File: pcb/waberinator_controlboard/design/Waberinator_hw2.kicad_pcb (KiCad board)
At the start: 2 copper layers, 104 parts, among them J1 Conn_01x04_Pin, J11 Strang 1, J12 Strang 2, J13 Strang 3, J14 Strang 4, J15 Strang 5, J16 Strang 6, J4 Conn_01x08_Pin, Q1 AOSP21321, Q2 SISHA04DN-T1-GE3, Q3 SISHA04DN-T1-GE3, Q4 SISHA04DN-T1-GE3, Q5 SISHA04DN-T1-GE3, Q6 SISHA04DN-T1-GE3, Q7 SISHA04DN-T1-GE3, SW1 SW_SPDT, SW2 SW_SPDT, U1 STM32F030R8Tx, U2 AMS1117-3.3, U3 LM73606QRNPRQ1, U4 LM75B, U5 MCP14A0304xMNY, U6 MCP14A0304xMNY, U7 MCP14A0304xMNY

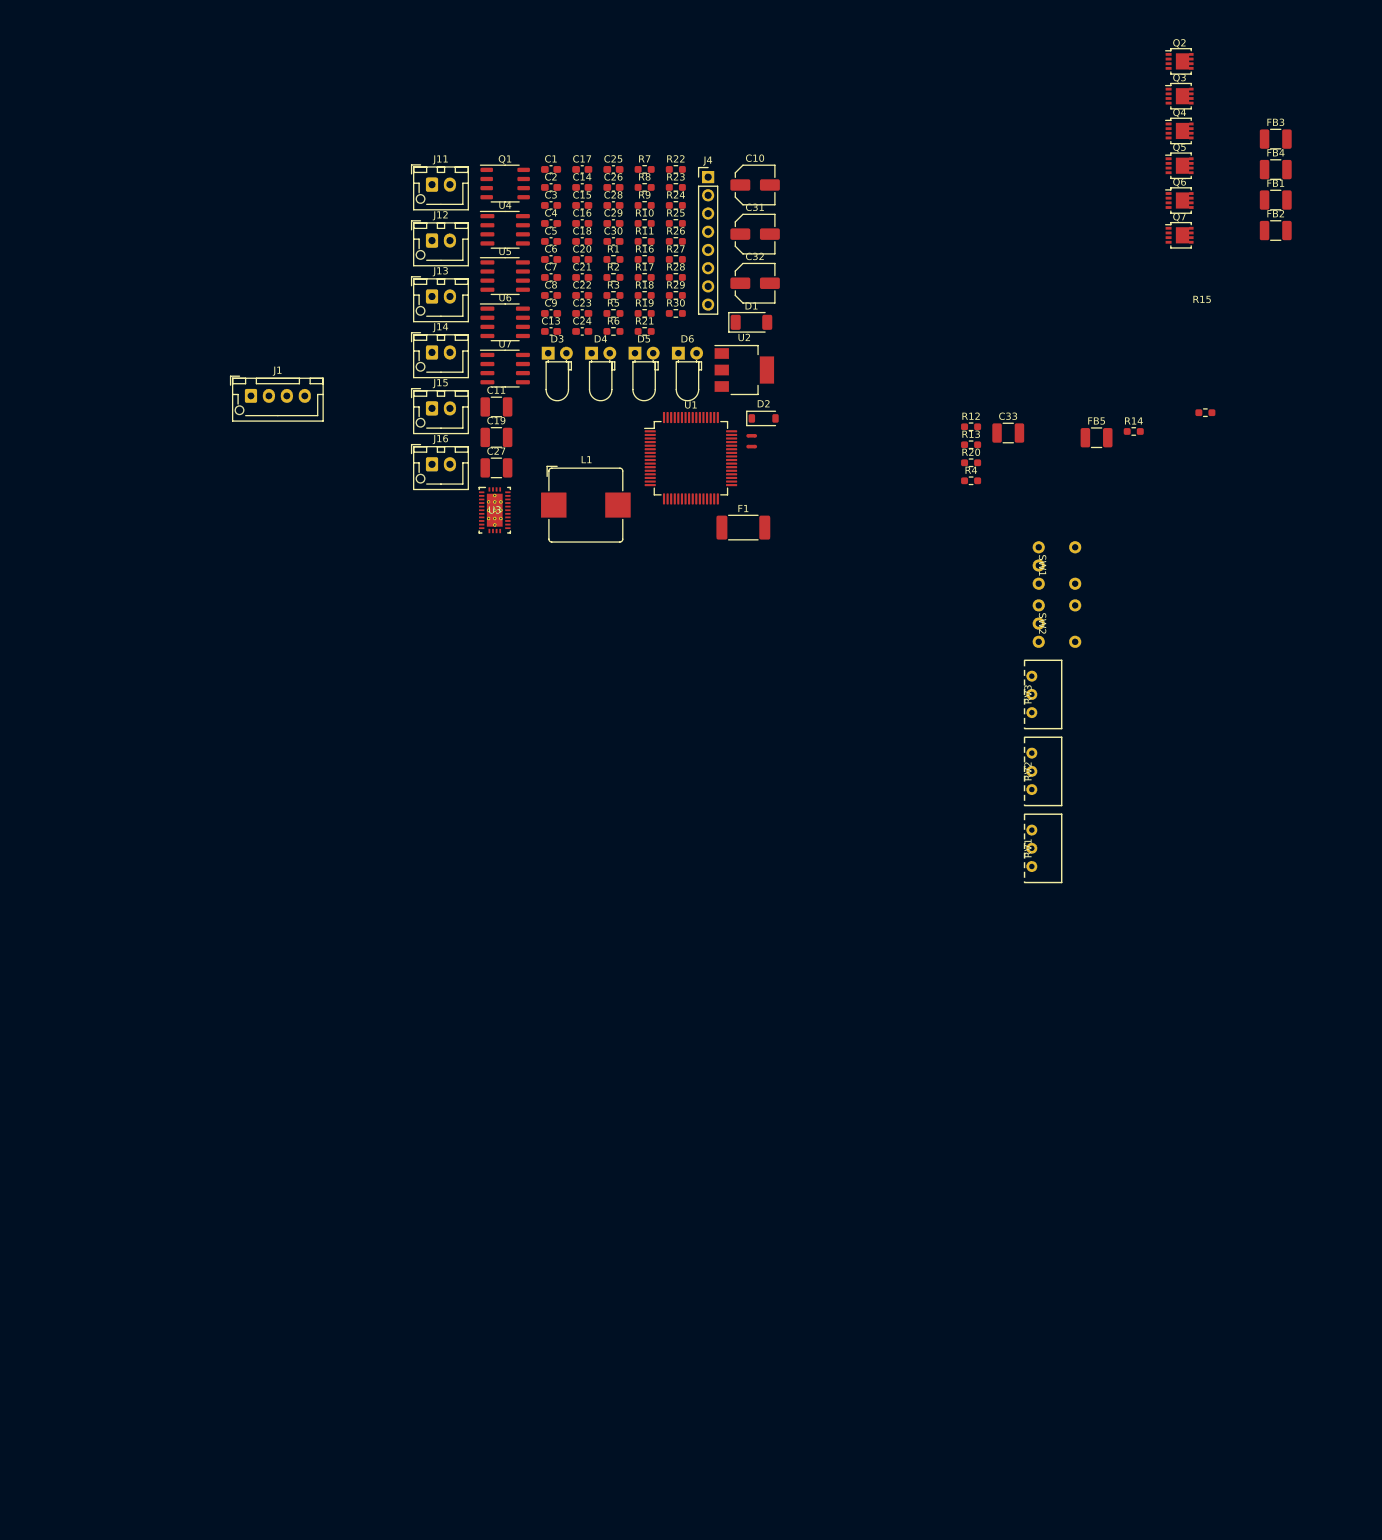
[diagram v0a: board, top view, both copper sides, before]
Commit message: [PCB] components roughly placed
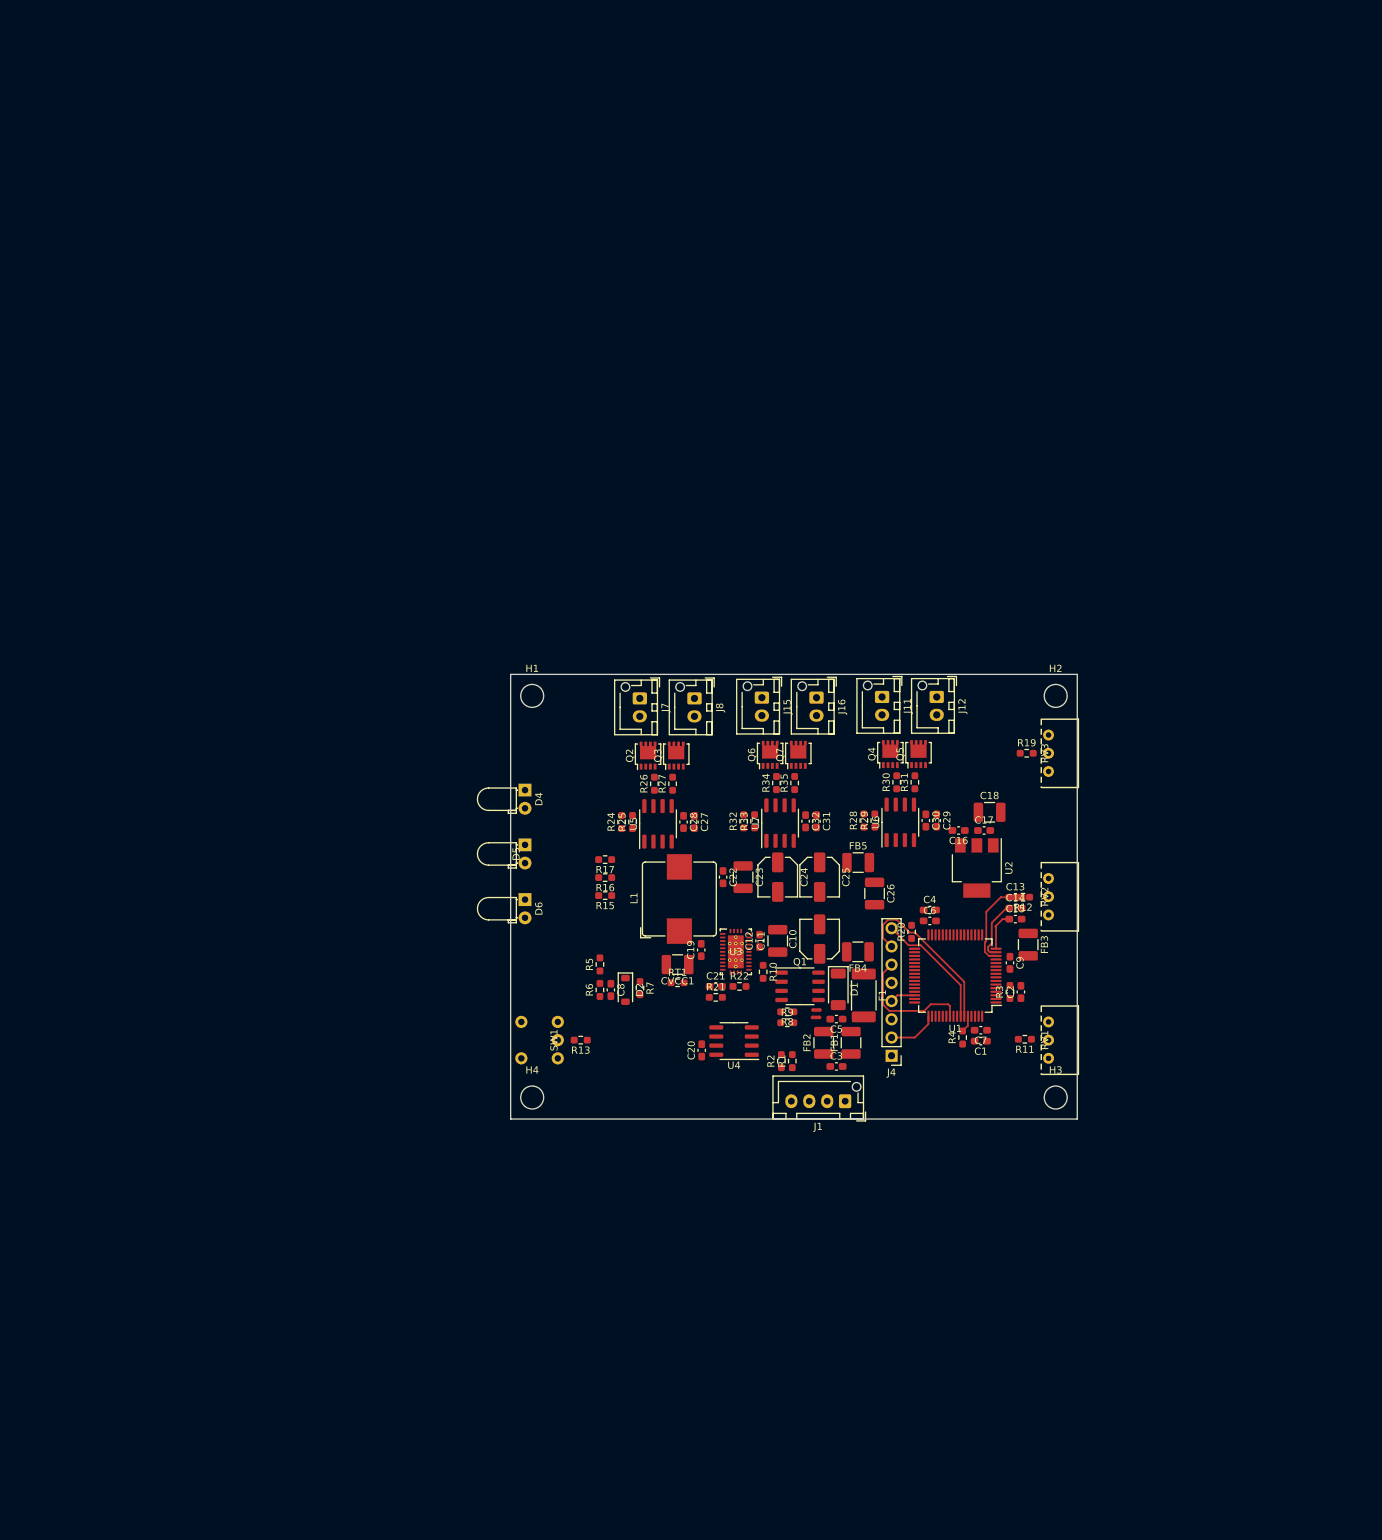
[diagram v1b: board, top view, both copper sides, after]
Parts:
- removed the C24 at (99.0, 68.2)
- removed the C25 at (103.3, 45.6)
- removed the C26 at (103.3, 48.1)
- removed D3: LED, LED_THT:LED_D3.0mm_Horizontal_O1.27mm_Z2.0mm
- removed J13: Strang 3, Connector_JST:JST_XH_B2B-XH-AM_1x02_P2.50mm_Vertical
- removed J14: Strang 4, Connector_JST:JST_XH_B2B-XH-AM_1x02_P2.50mm_Vertical
- removed the R15 at (185.9, 79.5)
- removed the R19 at (107.7, 65.7)
- removed SW2: SW_SPDT, g7_hmi:switch_800usp8p1a1m6re
- added C27: 1µF, Capacitor_SMD:C_0603_1608Metric_Pad1.08x0.95mm_HandSolder, F.Cu at (114.6, 136.6)
- added C31: 1µF, Capacitor_SMD:C_0603_1608Metric_Pad1.08x0.95mm_HandSolder, F.Cu at (131.6, 136.5)
- added C32: 100nF, Capacitor_SMD:C_0603_1608Metric_Pad1.08x0.95mm_HandSolder, F.Cu at (130.1, 136.5)
- added CVCC1: 2.2µF, Capacitor_SMD:C_1210_3225Metric_Pad1.33x2.70mm_HandSolder, F.Cu at (112.3, 156.5)
- added H1: MountingHole, MountingHole:MountingHole_3.2mm_M3_DIN965, F.Cu at (92.0, 119.0)
- added H2: MountingHole, MountingHole:MountingHole_3.2mm_M3_DIN965, F.Cu at (165.0, 119.0)
- added H3: MountingHole, MountingHole:MountingHole_3.2mm_M3_DIN965, F.Cu at (165.0, 175.0)
- added H4: MountingHole, MountingHole:MountingHole_3.2mm_M3_DIN965, F.Cu at (92.0, 175.0)
- added J7: Strang A, Connector_JST:JST_XH_B2B-XH-AM_1x02_P2.50mm_Vertical, F.Cu at (107.0, 119.4)
- added J8: Strang B, Connector_JST:JST_XH_B2B-XH-AM_1x02_P2.50mm_Vertical, F.Cu at (114.6, 119.4)
- added R31: 1, Resistor_SMD:R_0603_1608Metric_Pad0.98x0.95mm_HandSolder, F.Cu at (145.4, 131.0)
- added R32: 1, Resistor_SMD:R_0603_1608Metric_Pad0.98x0.95mm_HandSolder, F.Cu at (121.5, 136.5)
- added R33: 1, Resistor_SMD:R_0603_1608Metric_Pad0.98x0.95mm_HandSolder, F.Cu at (123.0, 136.5)
- added R34: 1, Resistor_SMD:R_0603_1608Metric_Pad0.98x0.95mm_HandSolder, F.Cu at (126.1, 131.1)
- added R35: 1, Resistor_SMD:R_0603_1608Metric_Pad0.98x0.95mm_HandSolder, F.Cu at (128.6, 131.1)
- C29: value 100nF -> 1µF
- J11: value Strang 1 -> Strang A
- J12: value Strang 2 -> Strang B
- J15: value Strang 5 -> Strang A
- J16: value Strang 6 -> Strang B
- moved C1 135.5 mm to (154.6, 167.1), turned to 180 degrees
- moved FB1 131.6 mm to (136.5, 167.4), turned to 90 degrees
- moved C2 129.9 mm to (160.1, 160.3), turned to 90 degrees
- moved FB2 129.6 mm to (132.6, 167.4), turned to 90 degrees
- moved J1 128.6 mm to (135.6, 175.5), turned to 180 degrees
- moved C3 126.5 mm to (134.4, 170.7)
- moved J4 125.2 mm to (142.1, 169.2), turned to 180 degrees
- moved FB4 123.7 mm to (137.4, 154.7), turned to 180 degrees
- moved Q2 121.9 mm to (108.2, 127.3), turned to 90 degrees
- moved C7 120.9 mm to (154.6, 165.6), turned to 180 degrees
- moved Q1 119.2 mm to (129.3, 159.5)
- moved U4 117.5 mm to (120.1, 167.1), turned to 180 degrees
- moved FB3 117.5 mm to (161.2, 153.7), turned to -90 degrees
- moved R8 116.7 mm to (127.6, 163.1), turned to 180 degrees
- moved C13 116.0 mm to (159.4, 147.1)
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- renumbered C13 to C12, C14 to C13, C15 to C14, C16 to C15, C17 to C16, C18 to C17, C19 to C18, C20 to C19, C21 to C20, C22 to C21, C23 to C22, C27 to C23, C31 to C24, C32 to C25, C33 to C26, R12 to R11, R13 to R12, R14 to R13, R16 to R15, R17 to R16, R18 to R17, R20 to R19, R21 to R20, R22 to R21, R23 to R22, R11 to RT1
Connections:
- net Net-(C10-Pad1) renamed /lm_vin
- net Net-(C20-Pad2) renamed /lm_sw
- net Net-(U3-FB) renamed /lm_fb
- net Net-(U3-RT) renamed /lm_rt
- J11 pad 2: Net-(J11-Pin_2) -> /Two Strings1/low_a
- J12 pad 2: Net-(J12-Pin_2) -> /Two Strings1/low_b
- J15 pad 2: Net-(J15-Pin_2) -> /Two Strings2/low_a
- J16 pad 2: Net-(J16-Pin_2) -> /Two Strings2/low_b
- Q2 pad 1: Net-(Q2-G) -> RET
- Q2 pad 2: Net-(J11-Pin_2) -> RET
- Q2 pad 4: (no net) -> /Two Strings/gate_a
- Q2 pad 5: (no net) -> /Two Strings/low_a
- Q3 pad 1: Net-(Q3-G) -> RET
- Q3 pad 2: Net-(J12-Pin_2) -> RET
- Q3 pad 4: (no net) -> /Two Strings/gate_b
- Q3 pad 5: (no net) -> /Two Strings/low_b
- Q4 pad 1: Net-(Q4-G) -> RET
- Q4 pad 2: Net-(J13-Pin_2) -> RET
- Q4 pad 4: (no net) -> /Two Strings1/gate_a
- Q4 pad 5: (no net) -> /Two Strings1/low_a
- Q5 pad 1: Net-(Q5-G) -> RET
- Q5 pad 2: Net-(J14-Pin_2) -> RET
- Q5 pad 4: (no net) -> /Two Strings1/gate_b
- Q5 pad 5: (no net) -> /Two Strings1/low_b
- Q6 pad 1: Net-(Q6-G) -> RET
- Q6 pad 2: Net-(J15-Pin_2) -> RET
- Q6 pad 4: (no net) -> /Two Strings2/gate_a
- Q6 pad 5: (no net) -> /Two Strings2/low_a
- Q7 pad 1: Net-(Q7-G) -> RET
- Q7 pad 2: Net-(J16-Pin_2) -> RET
- Q7 pad 4: (no net) -> /Two Strings2/gate_b
- Q7 pad 5: (no net) -> /Two Strings2/low_b
- R24 pad 1: Net-(U5-OUTA) -> /tim3_ch1_ledstring1
- R24 pad 2: Net-(Q2-G) -> /Two Strings/out_a
- R25 pad 1: Net-(U5-OUTB) -> /tim3_ch2_ledstring2
- R25 pad 2: Net-(Q3-G) -> /Two Strings/out_b
- R26 pad 1: Net-(U6-OUTA) -> /Two Strings/out_a
- R26 pad 2: Net-(Q4-G) -> /Two Strings/gate_a
- R27 pad 1: Net-(U6-OUTB) -> /Two Strings/out_b
- R27 pad 2: Net-(Q5-G) -> /Two Strings/gate_b
- R28 pad 1: Net-(U7-OUTA) -> /tim3_ch3_ledstring3
- R28 pad 2: Net-(Q6-G) -> /Two Strings1/out_a
- R29 pad 1: Net-(U7-OUTB) -> /tim3_ch4_ledstring4
- R29 pad 2: Net-(Q7-G) -> /Two Strings1/out_b
- R30 pad 1: Net-(R30-Pad1) -> /Two Strings1/out_a
- R30 pad 2: unconnected-(R30-Pad2) -> /Two Strings1/gate_a
- U3 pad 7: Net-(U3-VCC) -> /lm_vcc
- U5 pad 5: Net-(U5-OUTB) -> /Two Strings/out_b
- U5 pad 7: Net-(U5-OUTA) -> /Two Strings/out_a
- U6 pad 5: Net-(U6-OUTB) -> /Two Strings1/out_b
- U6 pad 7: Net-(U6-OUTA) -> /Two Strings1/out_a
- U7 pad 5: Net-(U7-OUTB) -> /Two Strings2/out_b
- U7 pad 7: Net-(U7-OUTA) -> /Two Strings2/out_a
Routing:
- net /usart1_rx_mcu: track 0.00 -> 23.5 mm
- net /swd_swo: track 0.00 -> 17.6 mm
- net /usart1_tx_mcu: track 0.00 -> 17.3 mm
- net /adc_brightness: track 0.00 -> 11.5 mm
- net /adc_frequency: track 0.00 -> 8.56 mm
- net /swd_tck: track 0.00 -> 7.00 mm
- net /adc_depth: track 0.00 -> 5.50 mm
- net /swd_tms: track 0.00 -> 3.55 mm
- net /boot0: track 0.00 -> 2.35 mm
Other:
- board outline added: 79 x 62 mm

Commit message: [HW] draft chassis
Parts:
- removed D4, D5, D6: LED, LED_THT:LED_D3.0mm_Horizontal_O1.27mm_Z2.0mm
- added D3: RGB LED, LED_THT:LED_D5.0mm-4_RGB_Wide_Pins, F.Cu at (203.5, 69.8)
- added J17: Conn_01x01_Pin, g7_connectors:Chassis_Connector, F.Cu at (168.5, 163.3)
- added J18: Conn_01x01_Pin, g7_connectors:Chassis_Connector, F.Cu at (125.5, 120.5)
- added J19: Conn_01x01_Pin, g7_connectors:Chassis_Connector, F.Cu at (125.5, 143.5)
- added J20: Conn_01x01_Pin, g7_connectors:Chassis_Connector, F.Cu at (184.0, 43.0)
- added J21: Conn_01x01_Pin, g7_connectors:Chassis_Connector, F.Cu at (152.0, 43.1)
- added J22: Conn_01x01_Pin, g7_connectors:Chassis_Connector, F.Cu at (125.5, 63.5)
- added J23: Conn_01x01_Pin, g7_connectors:Chassis_Connector, F.Cu at (125.5, 88.0)
- moved SW1 149.9 mm to (198.5, 58.0), turned to -90 degrees
- moved R13 148.1 mm to (199.0, 58.0)
- moved H1 123.0 mm to (202.5, 65.0)
- moved R15 118.9 mm to (199.0, 77.8)
- moved R16 118.9 mm to (199.0, 75.3)
- moved R17 118.9 mm to (199.0, 72.8)
- moved H4 116.7 mm to (202.0, 136.0)
- moved R7 109.5 mm to (165.2, 67.0), turned to 0 degrees
- moved D2 109.3 mm to (165.5, 69.0), turned to 0 degrees
- moved C8 108.7 mm to (165.5, 71.0), turned to 0 degrees
- moved R6 108.4 mm to (165.5, 72.6), turned to 180 degrees
- moved C20 107.6 mm to (197.8, 99.0), turned to 180 degrees
- moved H3 107.4 mm to (151.0, 68.5)
- moved U4 105.4 mm to (196.5, 94.5), turned to -90 degrees
- moved R5 103.4 mm to (161.9, 72.6), turned to 180 degrees
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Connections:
- U1 pad 30: /button2 -> unconnected-(U1-PB11-Pad30)
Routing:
- net /usart1_rx_mcu: track 23.5 -> 0.00 mm
- net /swd_swo: track 17.6 -> 0.00 mm
- net /usart1_tx_mcu: track 17.3 -> 0.00 mm
- net /swd_tck: track 7.00 -> 0.00 mm
- net /swd_tms: track 3.55 -> 0.00 mm
- net /boot0: track 2.35 -> 0.00 mm
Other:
- board size 79 x 62 mm -> 57.5 x 99.5 mm
